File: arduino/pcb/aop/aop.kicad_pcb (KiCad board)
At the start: 2 copper layers, 11 parts, among them J1 Conn_01x02_Pin, M1 RFID-RC522, Q1 AO4435, SW1 SW_Push, U1 ESP32-C3_SUPERMINI_TH, U2 TC00500

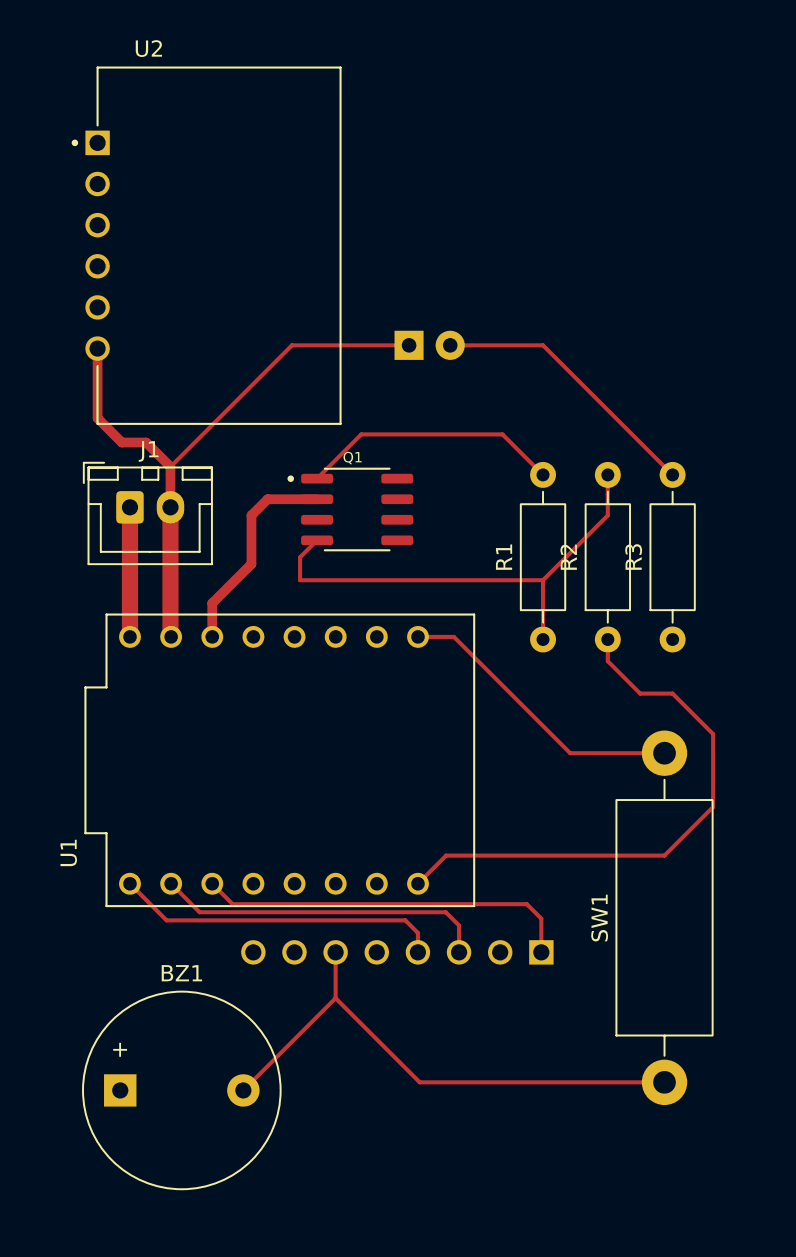
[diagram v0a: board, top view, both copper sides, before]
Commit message: One-sided tracing
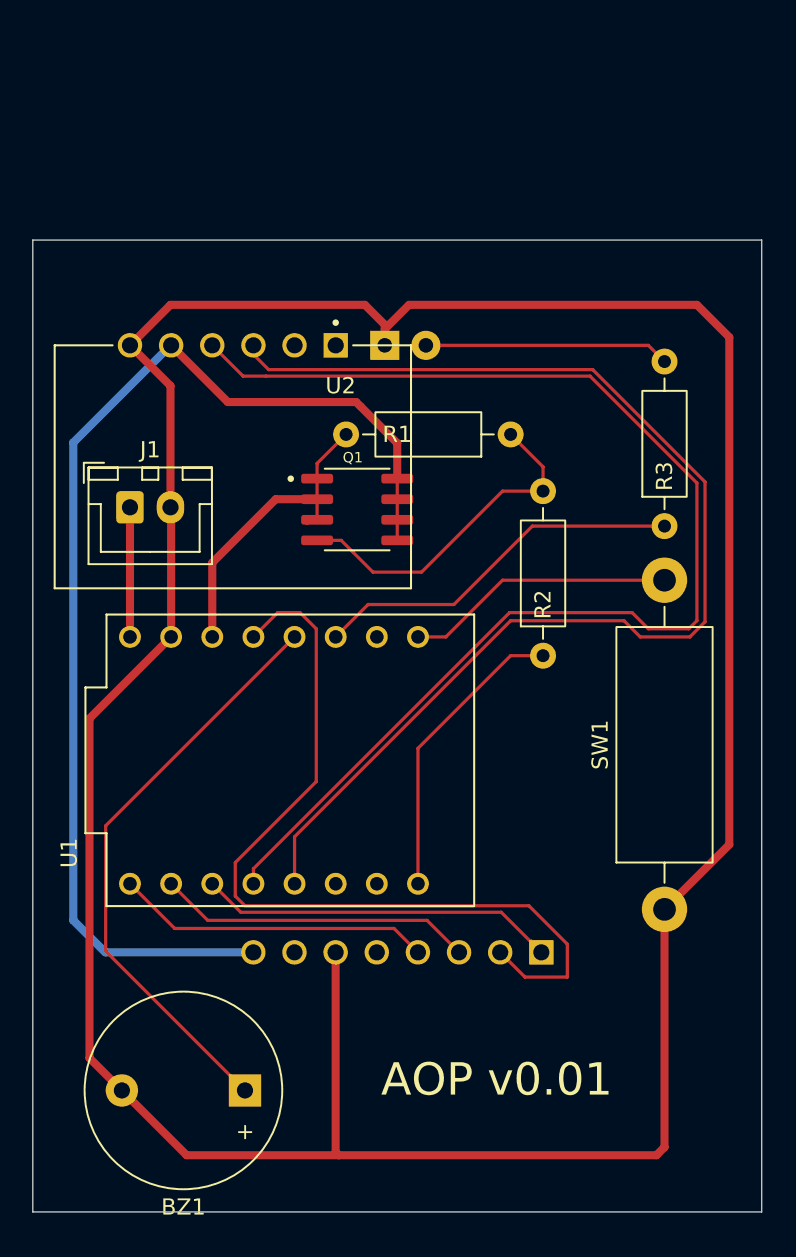
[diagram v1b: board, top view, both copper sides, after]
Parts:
- moved R1 12.8 mm to (99.0, 85.5), turned to 180 degrees
- moved SW1 10.7 mm to (108.5, 114.8)
- moved U2 10.4 mm to (81.8, 80.0), turned to -90 degrees
- moved BZ1 7.70 mm to (82.6, 126.0), turned to 180 degrees
- moved R3 7.02 mm to (108.5, 91.2)
- moved R2 4.12 mm to (101.0, 99.2)
- moved D1 1.50 mm to (91.2, 80.0)
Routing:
- net GND: track 71.7 -> 190.9 mm
- net Net-(U1-GPIO8): track 0.00 -> 77.4 mm
- net Net-(U1-GPIO9): track 0.00 -> 74.9 mm
- net +3.3VA: track 0.00 -> 72.4 mm
- net Net-(M1-SCK): track 0.00 -> 52.0 mm
- net Net-(BZ1-+): track 0.00 -> 36.4 mm
- net Net-(U1-GPIO2): track 0.00 -> 23.1 mm
- net Net-(U1-GPIO21): track 34.4 -> 18.4 mm
- net Net-(U1-3V3): track 29.1 -> 19.5 mm
- net Net-(Q1-Pad4): track 29.7 -> 21.2 mm
- net Net-(D1-A): track 17.0 -> 14.4 mm
- net Net-(U1-GPIO0): track 18.2 -> 16.7 mm
- net Net-(M1-MOSI): track 20.5 -> 19.5 mm
- net Net-(M1-MISO): track 20.2 -> 19.5 mm
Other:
- board outline added: 45 x 60 mm
- board text added: "AOP v0.01"

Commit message: Ordered PCB v0.2
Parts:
- added ?: , , F.Cu at (104.5, 89.0)
- added ?: , , F.Cu at (104.5, 124.0)
- Q1: moved to B.Cu
- moved R1 2.08 mm to (101.1, 85.5)
- moved U1 1.00 mm to (85.4, 104.6)
- turned Q1 to 180 degrees
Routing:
- net GND: track 190.9 -> 156.9 mm
- net +3.3VA: track 72.4 -> 104.7 mm
- net Net-(Q1-Pad4): track 21.2 -> 13.8 mm
- net Net-(U1-3V3): track 19.5 -> 22.9 mm
- net Net-(U1-GPIO21): track 18.4 -> 16.3 mm
- net Net-(BZ1-+): track 36.4 -> 37.5 mm
- net +BATT: track 8.00 -> 7.00 mm
- net Net-(M1-MOSI): track 19.5 -> 20.5 mm
- net Net-(U1-GPIO8): track 77.4 -> 76.6 mm
- net Net-(M1-SCK): track 52.0 -> 52.6 mm
- net Net-(U1-GPIO9): track 74.9 -> 74.3 mm
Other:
- board text added: "AOP v0.02"
- board text removed: "AOP v0.01"

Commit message: Try two-layer PCB
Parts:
- SW1: footprint Resistor_THT:R_Axial_DIN0614_L14.3mm_D5.7mm_P20.32mm_Horizontal -> Resistor_THT:R_Axial_DIN0414_L11.9mm_D4.5mm_P15.24mm_Horizontal
- moved SW1 5.08 mm to (108.5, 109.7)
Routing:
- net Net-(M1-SCK): track 52.6 -> 30.3 mm
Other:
- board text added: "AOP v0.03"
- board text removed: "AOP v0.02"
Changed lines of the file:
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@@
 			(drillshape 0)
 			(scaleselection 1)
-			(outputdirectory "/home/sakhnik/work/orienteering/arduin-o-punch/arduino/pcb/aop/0_02/")
+			(outputdirectory "/home/sakhnik/work/orienteering/arduin-o-punch/arduino/pcb/aop/0_03/")
 		)
 	)
@@
 		(property "Value" "1K"
 			(at 7.16 0 90)
-			(layer "F.Fab")
+			(layer "F.SilkS")
 			(effects
 				(font
@@
 		)
 		(property "Value" "ESP32-C3_SUPERMINI_TH"
-			(at 0 0 180)
+			(at 8.89 12.3825 90)
 			(layer "F.Fab")
 			(effects
@@
 		(property "Value" "100"
 			(at 6.58 0 90)
-			(layer "F.Fab")
+			(layer "F.SilkS")
 			(effects
 				(font
@@
 		(property "Value" "100K"
 			(at 4 0 0)
-			(layer "F.Fab")
+			(layer "F.SilkS")
 			(effects
 				(font
@@
 		)
 	)
-	(footprint "Resistor_THT:R_Axial_DIN0614_L14.3mm_D5.7mm_P20.32mm_Horizontal"
+	(footprint "Resistor_THT:R_Axial_DIN0414_L11.9mm_D4.5mm_P15.24mm_Horizontal"
 		(layer "F.Cu")
-		(at 108.5 114.82 90)
-		(descr "Resistor, Axial_DIN0614 series, Axial, Horizontal, pin pitch=20.32mm, 1.5W, length*diameter=14.3*5.7mm^2")
-		(tags "Resistor Axial_DIN0614 series Axial Horizontal pin pitch 20.32mm 1.5W length 14.3mm diameter 5.7mm")
+		(at 108.5 109.74 90)
+		(descr "Resistor, Axial_DIN0414 series, Axial, Horizontal, pin pitch=15.24mm, 2W, length*diameter=11.9*4.5mm^2, http://www.vishay.com/docs/20128/wkxwrx.pdf")
+		(tags "Resistor Axial_DIN0414 series Axial Horizontal pin pitch 15.24mm 2W length 11.9mm diameter 4.5mm")
 		(property "Reference" "SW1"
-			(at 10.16 -3.97 90)
+			(at 7.62 -3.37 90)
 			(layer "F.SilkS")
 			(effects
@@
 		)
 		(property "Value" "SW_Push"
-			(at 10.16 3.97 90)
+			(at 7.62 3.37 90)
 			(layer "F.Fab")
 			(effects
@@
 		(attr through_hole)
 		(fp_line
-			(start 18.68 0)
-			(end 17.43 0)
+			(start 13.8 0)
+			(end 13.69 0)
 			(stroke
 				(width 0.12)
@@
 		)
 		(fp_line
-			(start 1.64 0)
-			(end 2.89 0)
+			(start 1.44 0)
+			(end 1.55 0)
 			(stroke
 				(width 0.12)
@@
 		)
 		(fp_rect
-			(start 2.89 -2.97)
-			(end 17.43 2.97)
+			(start 1.55 -2.37)
+			(end 13.69 2.37)
 			(stroke
 				(width 0.12)
@@
 		)
 		(fp_rect
-			(start -1.65 -3.1)
-			(end 21.97 3.1)
+			(start -1.45 -2.5)
+			(end 16.69 2.5)
 			(stroke
 				(width 0.05)
@@
 		)
 		(fp_line
-			(start 20.32 0)
-			(end 17.31 0)
+			(start 15.24 0)
+			(end 13.57 0)
 			(stroke
 				(width 0.1)
@@
 		(fp_line
 			(start 0 0)
-			(end 3.01 0)
+			(end 1.67 0)
 			(stroke
 				(width 0.1)
@@
 		)
 		(fp_rect
-			(start 3.01 -2.85)
-			(end 17.31 2.85)
+			(start 1.67 -2.25)
+			(end 13.57 2.25)
 			(stroke
 				(width 0.1)
@@
 		)
 		(fp_text user "${REFERENCE}"
-			(at 10.16 0 90)
+			(at 7.62 0 90)
 			(layer "F.Fab")
 			(effects
@@
 		(pad "1" thru_hole circle
 			(at 0 0 90)
-			(size 2.8 2.8)
-			(drill 1.4)
+			(size 1.6 1.6)
+			(drill 0.8)
 			(layers "*.Cu" "*.Mask")
 			(remove_unused_layers no)
@@
 		)
 		(pad "2" thru_hole circle
-			(at 20.32 0 90)
-			(size 2.8 2.8)
-			(drill 1.4)
+			(at 15.24 0 90)
+			(size 1.6 1.6)
+			(drill 0.8)
 			(layers "*.Cu" "*.Mask")
 			(remove_unused_layers no)
@@
 		)
 		(embedded_fonts no)
-		(model "${KICAD9_3DMODEL_DIR}/Resistor_THT.3dshapes/R_Axial_DIN0614_L14.3mm_D5.7mm_P20.32mm_Horizontal.step"
+		(model "${KICAD9_3DMODEL_DIR}/Resistor_THT.3dshapes/R_Axial_DIN0414_L11.9mm_D4.5mm_P15.24mm_Horizontal.step"
 			(offset
 				(xyz 0 0 0)
@@
 		(descr "MFRC522 RFID Module<br><br>Created by: Wai Weng")
 		(property "Reference" "M1"
-			(at 0.0054 -2.0256 0)
+			(at 0 0 0)
 			(layer "B.SilkS")
 			(effects
@@
 		(layer "Edge.Cuts")
 	)
-	(gr_text "AOP v0.02"
-		(at 101.5 129.5 0)
-		(layer "B.Cu")
+	(gr_text "AOP v0.03"
+		(at 90.5 129.5 0)
+		(layer "F.SilkS")
 		(effects
 			(font
-				(size 1.5 1.5)
+				(size 2 2)
 				(thickness 0.3)
-				(bold yes)
 			)
-			(justify left bottom mirror)
+			(justify left bottom)
 		)
 	)
 	(segment
+		(start 108.5 109.5)
+		(end 108.5 120.5)
+		(width 0.5)
+		(layer "B.Cu")
+		(net 1)
+	)
+	(segment
 		(start 91.23 79)
 		(end 91.23 80)
@@
 	)
 	(segment
+		(start 112.5 105.5)
+		(end 108.5 109.5)
+		(width 0.5)
+		(layer "B.Cu")
+		(net 1)
+	)
+	(segment
 		(start 88.1954 120.1954)
-		(end 89 121)
+		(end 88.1954 117.4744)
 		(width 0.5)
 		(layer "B.Cu")
@@
 	)
 	(segment
-		(start 110.5 77.5)
-		(end 112.5 79.5)
+		(start 108.5 120.5)
+		(end 108 121)
 		(width 0.5)
 		(layer "B.Cu")
@@
 	)
 	(segment
-		(start 112.5 110.82)
-		(end 108.5 114.82)
+		(start 89 121)
+		(end 88.1954 120.1954)
 		(width 0.5)
 		(layer "B.Cu")
@@
 	)
 	(segment
-		(start 91.23 79)
-		(end 92.73 77.5)
-		(width 0.5)
-		(layer "B.Cu")
-		(net 1)
-	)
-	(segment
-		(start 88.1954 117.4744)
-		(end 88.1954 120.1954)
+		(start 91.23 78.73)
+		(end 91.23 79)
 		(width 0.5)
 		(layer "B.Cu")
@@
 	)
 	(segment
-		(start 91.23 78.73)
-		(end 91.23 79)
+		(start 91.23 79)
+		(end 92.73 77.5)
 		(width 0.5)
 		(layer "B.Cu")
@@
 	)
 	(segment
-		(start 112.5 79.5)
-		(end 112.5 110.82)
-		(width 0.5)
-		(layer "B.Cu")
-		(net 1)
-	)
-	(segment
-		(start 108 121)
-		(end 108.5 120.5)
+		(start 90 77.5)
+		(end 91.23 78.73)
 		(width 0.5)
 		(layer "B.Cu")
@@
 	)
 	(segment
-		(start 90 77.5)
-		(end 91.23 78.73)
+		(start 110.5 77.5)
+		(end 112.5 79.5)
 		(width 0.5)
 		(layer "B.Cu")
@@
 	)
 	(segment
-		(start 108.5 120.5)
-		(end 108.5 114.82)
+		(start 78.04 90.54)
+		(end 78.04 98)
 		(width 0.5)
 		(layer "B.Cu")
@@
 	)
 	(segment
-		(start 92.73 77.5)
-		(end 110.5 77.5)
+		(start 78.04 98)
+		(end 73 103.04)
 		(width 0.5)
 		(layer "B.Cu")
@@
 	)
 	(segment
-		(start 78.04 90.54)
-		(end 78.04 98)
+		(start 108 121)
+		(end 89 121)
 		(width 0.5)
 		(layer "B.Cu")
@@
 	)
 	(segment
-		(start 78.04 98)
-		(end 73 103.04)
+		(start 112.5 79.5)
+		(end 112.5 105.5)
 		(width 0.5)
 		(layer "B.Cu")
@@
 	)
 	(segment
-		(start 89 121)
-		(end 108 121)
+		(start 92.73 77.5)
+		(end 110.5 77.5)
 		(width 0.5)
 		(layer "B.Cu")
@@
 	)
 	(segment
-		(start 87 96.5)
-		(end 87 106.384504)
-		(width 0.3)
-		(layer "B.Cu")
-		(net 7)
-	)
-	(segment
-		(start 83.12 97)
-		(end 84.62 95.5)
-		(width 0.3)
-		(layer "B.Cu")
-		(net 7)
-	)
-	(segment
-		(start 102.5 119)
-		(end 99.881 119)
-		(width 0.3)
-		(layer "B.Cu")
-		(net 7)
-	)
-	(segment
-		(start 99.881 119)
-		(end 98.3554 117.4744)
+		(start 96 105.5)
+		(end 98.3554 107.8554)
 		(width 0.3)
-		(layer "B.Cu")
-		(net 7)
-	)
-	(segment
-		(start 84.62 95.5)
-		(end 86 95.5)
-		(width 0.3)
-		(layer "B.Cu")
-		(net 7)
-	)
-	(segment
-		(start 87 106.384504)
-		(end 81.995 111.389504)
-		(width 0.3)
-		(layer "B.Cu")
-		(net 7)
-	)
-	(segment
-		(start 82.899 113.899)
-		(end 99.73 113.899)
-		(width 0.3)
-		(layer "B.Cu")
-		(net 7)
-	)
-	(segment
-		(start 86 95.5)
-		(end 87 96.5)
-		(width 0.3)
-		(layer "B.Cu")
+		(layer "F.Cu")
 		(net 7)
 	)
 	(segment
-		(start 81.995 112.995)
-		(end 82.899 113.899)
+		(start 90 105.5)
+		(end 96 105.5)
 		(width 0.3)
-		(layer "B.Cu")
+		(layer "F.Cu")
 		(net 7)
 	)
 	(segment
-		(start 81.995 111.389504)
-		(end 81.995 112.995)
+		(start 83.12 97)
+		(end 83.12 98.62)
 		(width 0.3)
-		(layer "B.Cu")
+		(layer "F.Cu")
 		(net 7)
 	)
 	(segment
-		(start 102.5 116.669)
-		(end 102.5 119)
+		(start 83.12 98.62)
+		(end 90 105.5)
 		(width 0.3)
-		(layer "B.Cu")
+		(layer "F.Cu")
 		(net 7)
 	)
 	(segment
-		(start 99.73 113.899)
-		(end 102.5 116.669)
+		(start 98.3554 107.8554)
+		(end 98.3554 117.4744)
 		(width 0.3)
-		(layer "B.Cu")
+		(layer "F.Cu")
 		(net 7)
 	)

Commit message: [pcb] AOP v0.1
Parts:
- removed the ? at (104.5, 89.0)
- removed the ? at (104.5, 124.0)
- removed U1: ESP32-C3_SUPERMINI_TH, ESP32-C3_SUPERMINI_TH:MODULE_ESP32-C3_SUPERMINI_TH
- removed U2: TC00500, TC00500:MODULE_TC00500
- added ?: , , F.Cu at (80.0, 94.0)
- added ?: , , F.Cu at (82.5, 115.0)
- added ?: , , F.Cu at (75.0, 94.0)
- added ?: , , F.Cu at (82.5, 94.0)
- added ?: , , F.Cu at (87.5, 115.0)
- added ?: , , F.Cu at (87.5, 94.0)
- added ?: , , F.Cu at (75.0, 115.0)
- added ?: , , F.Cu at (90.0, 115.0)
- added ?: , , B.Cu at (72.5, 115.5)
- added ?: , , B.Cu at (90.0, 115.5)
- added ?: , , B.Cu at (75.0, 94.0)
- added ?: , , F.Cu at (90.0, 94.0)
- added ?: , , B.Cu at (72.5, 94.0)
- added ?: , , B.Cu at (75.0, 115.5)
- added ?: , , B.Cu at (90.5, 94.0)
- added ?: , , B.Cu at (77.5, 115.5)
- added ?: , , B.Cu at (82.5, 115.5)
- added ?: , , B.Cu at (80.0, 94.0)
- added ?: , , B.Cu at (77.5, 94.0)
- added ?: , , B.Cu at (80.0, 115.5)
- added ?: , , B.Cu at (87.5, 115.5)
- added ?: , , B.Cu at (88.0, 94.0)
- added ?: , , F.Cu at (77.5, 94.0)
- added ?: , , B.Cu at (85.0, 115.5)
- added ?: , , B.Cu at (82.5, 94.0)
- added ?: , , B.Cu at (85.0, 94.0)
- added ?: , , F.Cu at (77.5, 115.0)
- added ?: , , F.Cu at (72.5, 94.0)
- added ?: , , F.Cu at (85.0, 115.0)
- added ?: , , F.Cu at (85.0, 94.0)
- added ?: , , F.Cu at (72.5, 115.0)
- added ?: , , F.Cu at (80.0, 115.0)
- added SW2: SW_Push, Resistor_THT:R_Axial_DIN0414_L11.9mm_D4.5mm_P15.24mm_Horizontal, F.Cu at (110.5, 123.0)
- D1: footprint LED_THT:LED_D3.0mm -> LED_SMD:LED_1206_3216Metric; moved to F.Cu
- M1: footprint RFID-RC522:RFID-RC522 -> RFID-RC522:RFID-RC522_1; moved to F.Cu
- Q1: moved to F.Cu
- R1, R2, R3: footprint Resistor_THT:R_Axial_DIN0207_L6.3mm_D2.5mm_P10.16mm_Horizontal -> Resistor_SMD:R_1206_3216Metric
- SW1: footprint Resistor_THT:R_Axial_DIN0414_L11.9mm_D4.5mm_P15.24mm_Horizontal -> Resistor_THT:R_Axial_DIN0207_L6.3mm_D2.5mm_P5.08mm_Vertical
- moved BZ1 53.2 mm to (104.5, 77.5), turned to -90 degrees
- moved M1 12.3 mm to (81.0, 123.0)
- moved R2 8.26 mm to (104.0, 91.5), turned to -90 degrees
- moved R1 6.74 mm to (98.0, 91.5), turned to 90 degrees
- moved SW1 6.74 mm to (106.0, 116.0), turned to 180 degrees
- moved J1 5.85 mm to (77.5, 84.5), turned to 180 degrees
- moved Q1 4.23 mm to (87.5, 86.4), turned to 0 degrees
- moved R3 1.04 mm to (109.5, 91.5)
- moved D1 1.00 mm to (92.1, 79.5)
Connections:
- BZ1 pad 1: Net-(BZ1-+) -> +BATT
- BZ1 pad 2: GND -> Net-(BZ1--)
- D1 pad 1: GND -> +BATT
- Q1 pad 1: Net-(U1-3V3) -> +BATT
- Q1 pad 2: Net-(U1-3V3) -> +BATT
- Q1 pad 3: Net-(U1-3V3) -> +BATT
- R1 pad 2: Net-(U1-3V3) -> +BATT
- R2 pad 1: Net-(U1-GPIO21) -> Net-(Q1-Pad4)
- R2 pad 2: Net-(Q1-Pad4) -> Net-(U1-GPIO21)
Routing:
- net Net-(U1-GPIO8): track 76.6 -> 0.00 mm
- net Net-(U1-GPIO9): track 74.3 -> 0.00 mm
- net +BATT: track 7.00 -> 58.1 mm
- net Net-(BZ1-+): track 37.5 -> 0.00 mm
- net Net-(BZ1--): track 0.00 -> 29.4 mm
- net Net-(U1-GPIO0): track 16.3 -> 39.4 mm
- net Net-(U1-3V3): track 22.9 -> 0.00 mm
- net Net-(M1-SCK): track 30.3 -> 51.8 mm, vias 0 -> 1
- net GND: track 156.9 -> 140.2 mm
- net Net-(U1-GPIO21): track 16.3 -> 31.5 mm
- net Net-(U1-GPIO2): track 23.4 -> 35.0 mm, vias 0 -> 1
- net Net-(D1-A): track 14.4 -> 23.3 mm
- net Net-(Q1-Pad4): track 13.8 -> 22.5 mm
- net +3.3VA: track 104.7 -> 111.9 mm, vias 0 -> 2
- net Net-(M1-SDA): track 23.3 -> 17.6 mm
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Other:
- board size 45 x 60 mm -> 45 x 54.5 mm
- board text added: "AOP v0.1"
- board text removed: "AOP v0.03"
